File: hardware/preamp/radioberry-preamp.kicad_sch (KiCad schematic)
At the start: 4 parts

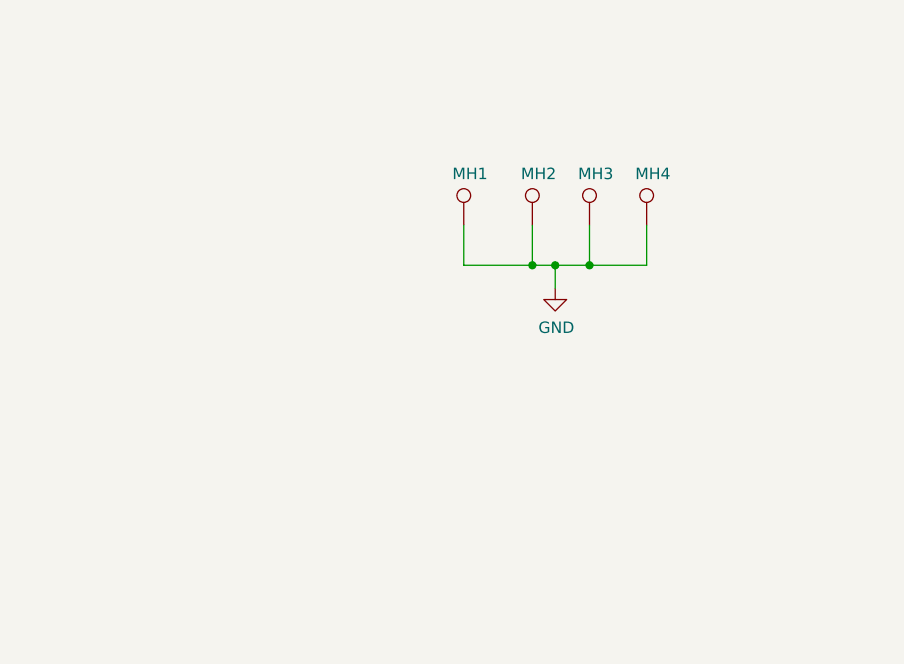
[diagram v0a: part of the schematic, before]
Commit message: kicad 8.0 conversion
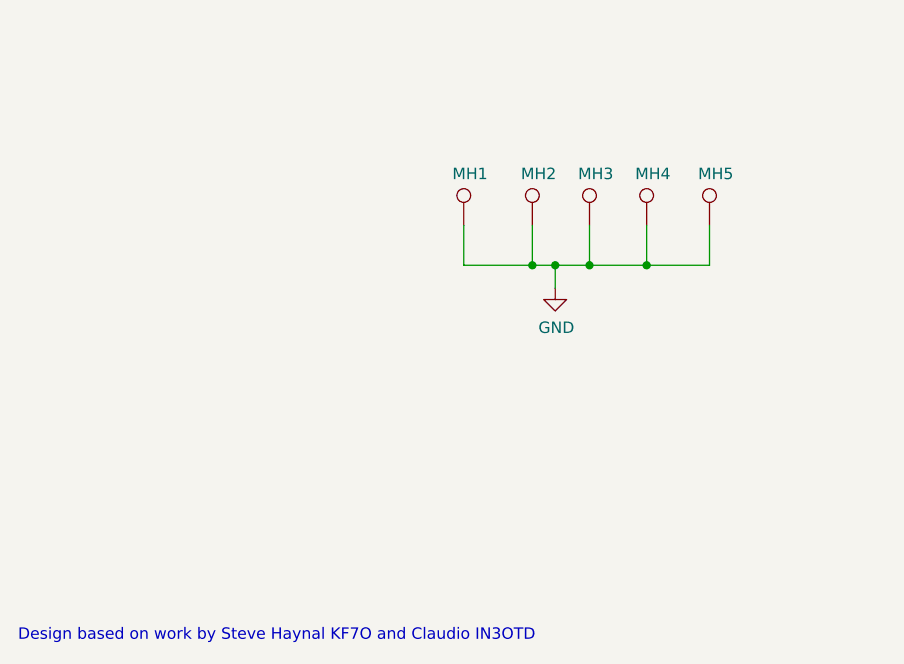
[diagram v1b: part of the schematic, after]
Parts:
- added MH5: DNI, HERMESLITE:m3, symbol hermeslite:TEST_1P
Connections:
- net GND: now also MH5.1
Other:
- note added: "Design based on work by Steve Haynal KF7O and Claudio IN3OTD"
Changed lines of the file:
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@@
+	)
+	(junction
+		(at 85.09 147.955)
+		(diameter 0)
+		(color 0 0 0 0)
+	)
+	(junction
+		(at 91.44 147.955)
+		(diameter 0)
+		(color 0 0 0 0)
+	)
+	(junction
+		(at 78.74 147.955)
+		(diameter 0)
+		(color 0 0 0 0)
 	)
 	(junction
@@
 		(color 0 0 0 0)
 	)
-	(junction
-		(at 78.74 147.955)
-		(diameter 0)
-		(color 0 0 0 0)
-	)
-	(junction
-		(at 85.09 147.955)
-		(diameter 0)
-		(color 0 0 0 0)
+	(wire
+		(pts
+			(xy 71.12 147.955) (xy 78.74 147.955)
+		)
+		(stroke
+			(width 0)
+			(type default)
+		)
+	)
+	(wire
+		(pts
+			(xy 78.74 143.51) (xy 78.74 147.955)
+		)
+		(stroke
+			(width 0)
+			(type default)
+		)
+	)
+	(wire
+		(pts
+			(xy 85.09 147.955) (xy 91.44 147.955)
+		)
+		(stroke
+			(width 0)
+			(type default)
+		)
+	)
+	(wire
+		(pts
+			(xy 98.425 147.955) (xy 98.425 143.51)
+		)
+		(stroke
+			(width 0)
+			(type default)
+		)
 	)
 	(wire
@@
 	(wire
 		(pts
-			(xy 71.12 147.955) (xy 78.74 147.955)
+			(xy 91.44 147.955) (xy 98.425 147.955)
+		)
+		(stroke
+			(width 0)
+			(type default)
+		)
+	)
+	(wire
+		(pts
+			(xy 78.74 147.955) (xy 81.28 147.955)
 		)
 		(stroke
@@
 	(wire
 		(pts
-			(xy 85.09 147.955) (xy 91.44 147.955)
-		)
-		(stroke
-			(width 0)
-			(type default)
-		)
-	)
-	(wire
-		(pts
-			(xy 78.74 147.955) (xy 81.28 147.955)
-		)
-		(stroke
-			(width 0)
-			(type default)
-		)
-	)
-	(wire
-		(pts
-			(xy 78.74 143.51) (xy 78.74 147.955)
+			(xy 81.28 147.955) (xy 85.09 147.955)
 		)
 		(stroke
@@
 		)
 	)
-	(wire
-		(pts
-			(xy 81.28 147.955) (xy 85.09 147.955)
-		)
-		(stroke
-			(width 0)
-			(type default)
+	(text "Design based on work by Steve Haynal KF7O and Claudio IN3OTD"
+		(exclude_from_sim no)
+		(at 21.59 189.865 0)
+		(effects
+			(font
+				(size 1.27 1.27)
+			)
+			(justify left bottom)
 		)
 	)
@@
 		)
 		(instances
-			(project "hat"
-				(path "/ba8e7a9c-7c3b-408c-ae14-10b9ecdea265"
+			(project ""
+				(path "/6d412791-b44e-4843-85b0-670d5f76b1b8"
 					(reference "MH1")
 					(unit 1)
@@
 		)
 		(instances
-			(project "hat"
-				(path "/ba8e7a9c-7c3b-408c-ae14-10b9ecdea265"
+			(project ""
+				(path "/6d412791-b44e-4843-85b0-670d5f76b1b8"
 					(reference "MH2")
 					(unit 1)
@@
 		)
 		(instances
-			(project "hat"
-				(path "/ba8e7a9c-7c3b-408c-ae14-10b9ecdea265"
+			(project ""
+				(path "/6d412791-b44e-4843-85b0-670d5f76b1b8"
 					(reference "MH3")
 					(unit 1)
@@
 		)
 		(instances
-			(project "hat"
-				(path "/ba8e7a9c-7c3b-408c-ae14-10b9ecdea265"
+			(project ""
+				(path "/6d412791-b44e-4843-85b0-670d5f76b1b8"
 					(reference "MH4")
 					(unit 1)
@@
 		)
 		(instances
-			(project "hat"
-				(path "/ba8e7a9c-7c3b-408c-ae14-10b9ecdea265"
+			(project ""
+				(path "/6d412791-b44e-4843-85b0-670d5f76b1b8"
 					(reference "#PWR0114")
+					(unit 1)
+				)
+			)
+		)
+	)
+	(symbol
+		(lib_id "hermeslite:TEST_1P")
+		(at 98.425 143.51 0)
+		(unit 1)
+		(exclude_from_sim no)
+		(in_bom yes)
+		(on_board yes)
+		(dnp no)
+		(property "Reference" "MH5"
+			(at 97.155 137.795 0)
+			(effects
+				(font
+					(size 1.27 1.27)
+				)
+				(justify left)
+			)
+		)
+		(property "Value" "DNI"
+			(at 99.8982 142.8242 0)
+			(effects
+				(font
+					(size 1.27 1.27)
+				)
+				(justify left)
+				(hide yes)
+			)
+		)
+		(property "Footprint" "HERMESLITE:m3"
+			(at 103.505 143.51 0)
+			(effects
+				(font
+					(size 1.27 1.27)
+				)
+				(hide yes)
+			)
+		)
+		(property "Datasheet" ""
+			(at 103.505 143.51 0)
+			(effects
+				(font
+					(size 1.27 1.27)
+				)
+				(hide yes)
+			)
+		)
+		(property "Description" ""
+			(at 98.425 143.51 0)
+			(effects
+				(font
+					(size 1.27 1.27)
+				)
+				(hide yes)
+			)
+		)
+		(property "Option" "DNI"
+			(at 98.425 143.51 0)
+			(effects
+				(font
+					(size 1.27 1.27)
+				)
+				(hide yes)
+			)
+		)
+		(property "Key" "NOBOM"
+			(at 98.425 143.51 0)
+			(effects
+				(font
+					(size 1.27 1.27)
+				)
+				(hide yes)
+			)
+		)
+		(pin "1"
+		)
+		(instances
+			(project ""
+				(path "/6d412791-b44e-4843-85b0-670d5f76b1b8"
+					(reference "MH5")
 					(unit 1)
 				)
@@
 		)
 		(instances
-			(project "hat"
-				(path "/ba8e7a9c-7c3b-408c-ae14-10b9ecdea265"
+			(project "radioberry-preamp"
+				(path "/6d412791-b44e-4843-85b0-670d5f76b1b8"
 					(page "4")
 				)
@@
 		)
 		(instances
-			(project "hat"
-				(path "/ba8e7a9c-7c3b-408c-ae14-10b9ecdea265"
+			(project "radioberry-preamp"
+				(path "/6d412791-b44e-4843-85b0-670d5f76b1b8"
 					(page "3")
 				)
@@
 		)
 		(instances
-			(project "hat"
-				(path "/ba8e7a9c-7c3b-408c-ae14-10b9ecdea265"
+			(project "radioberry-preamp"
+				(path "/6d412791-b44e-4843-85b0-670d5f76b1b8"
 					(page "2")
 				)
